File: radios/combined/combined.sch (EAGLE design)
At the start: 20 parts

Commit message: redesigned radios breakout
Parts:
- removed C1: 10uF, SparkFun-Capacitors:CAP_POL1206
- removed CONNECT, MODE: (no value), adafruit:LEDCHIPLED_0603
- removed DFU: (no value), wirepad:SMD2
- removed JP2: M11LONGPADS, SparkFun-Connectors:M11LONGPADS
- removed R1, R3: 1k, SparkFun-Resistors:RESISTOR0603
- added JP1: M11PTH, SparkFun-Connectors:M11PTH
- CLOCK, DATA, VCC: value (none) -> PAD; device wirepad:SMD2 -> ITP_Lab:PAD
- U$3: value 3.3V-REG-LARGE -> REGULATOR3.3V-UA78M33CDCYR; device ITP_Lab:3.3V-REG-LARGE -> ITP_Lab:REGULATOR3.3V-UA78M33CDCYR
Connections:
- removed net N$10: MODE.A, R3.1
- removed net N$13: DFU.P, U$4.P0.07
- removed net N$7: R1.2, U$4.P0.19
- removed net N$8: R3.2, U$4.P0.18
- removed net N$9: CONNECT.A, R1.1
- net BT-CTS: now also JP1.5; no longer JP2.10
- net BT-RTS: now also JP1.3; no longer JP2.8
- net BT-RX: now also JP1.6; no longer JP2.11
- net BT-TX: now also JP1.4; no longer JP2.9
- net GND: now also JP1.1; no longer C1.-, CONNECT.C, JP2.1, MODE.C
- net MISO: now also JP1.8; no longer JP2.4
- net MOSI: now also JP1.9; no longer JP2.5
- net N$11: now also CLOCK.P$1; no longer CLOCK.P
- net N$12: now also DATA.P$1; no longer DATA.P
- net RF-REQ: now also JP1.11; no longer JP2.7
- net RF-SS: now also JP1.10; no longer JP2.6
- net SCK: now also JP1.7; no longer JP2.3
- net VCC: now also VCC.P$1; no longer C1.+, VCC.P
- net VIN: now also JP1.2; no longer JP2.2

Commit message: about to cut board
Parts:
- removed JP1: M11PTH, SparkFun-Connectors:M11PTH
- added U$5: HEADER-11, ITP_Lab:HEADER-11
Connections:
- net BT-CTS: now also U$5.P$5; no longer JP1.5
- net BT-RTS: now also U$5.P$3; no longer JP1.3
- net BT-RX: now also U$5.P$6; no longer JP1.6
- net BT-TX: now also U$5.P$4; no longer JP1.4
- net GND: now also U$5.P$1; no longer JP1.1
- net MISO: now also U$5.P$8; no longer JP1.8
- net MOSI: now also U$5.P$9; no longer JP1.9
- net RF-REQ: now also U$5.P$11; no longer JP1.11
- net RF-SS: now also U$5.P$10; no longer JP1.10
- net SCK: now also U$5.P$7; no longer JP1.7
- net VIN: now also U$5.P$2; no longer JP1.2
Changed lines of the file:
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@@
 <part name="CLOCK" library="ITP_Lab" deviceset="PAD" device=""/>
 <part name="VCC" library="ITP_Lab" deviceset="PAD" device=""/>
-<part name="JP1" library="SparkFun-Connectors" deviceset="M11" device="PTH"/>
+<part name="U$5" library="ITP_Lab" deviceset="HEADER-11" device=""/>
 </parts>
 <sheets>
@@
 <instance part="CLOCK" gate="G$1" x="254" y="152.4"/>
 <instance part="VCC" gate="G$1" x="83.82" y="218.44" rot="R90"/>
-<instance part="JP1" gate="G$1" x="121.92" y="142.24" rot="R180"/>
+<instance part="U$5" gate="G$1" x="127" y="142.24"/>
 </instances>
 <busses>
@@
 </segment>
 <segment>
-<wire x1="111.76" y1="154.94" x2="86.36" y2="154.94" width="0.1524" layer="91"/>
+<wire x1="121.92" y1="154.94" x2="86.36" y2="154.94" width="0.1524" layer="91"/>
 <label x="93.98" y="154.94" size="1.778" layer="95" rot="R180"/>
-<pinref part="JP1" gate="G$1" pin="1"/>
+<pinref part="U$5" gate="G$1" pin="P$1"/>
 </segment>
 <segment>
@@
 <net name="VIN" class="0">
 <segment>
-<wire x1="111.76" y1="152.4" x2="86.36" y2="152.4" width="0.1524" layer="91"/>
+<wire x1="121.92" y1="152.4" x2="86.36" y2="152.4" width="0.1524" layer="91"/>
 <label x="93.98" y="152.4" size="1.778" layer="95" rot="R180"/>
-<pinref part="JP1" gate="G$1" pin="2"/>
+<pinref part="U$5" gate="G$1" pin="P$2"/>
 </segment>
 <segment>
@@
 </segment>
 <segment>
-<wire x1="111.76" y1="144.78" x2="86.36" y2="144.78" width="0.1524" layer="91"/>
+<wire x1="121.92" y1="144.78" x2="86.36" y2="144.78" width="0.1524" layer="91"/>
 <label x="93.98" y="144.78" size="1.778" layer="95" rot="R180"/>
-<pinref part="JP1" gate="G$1" pin="5"/>
+<pinref part="U$5" gate="G$1" pin="P$5"/>
 </segment>
 </net>
@@
 </segment>
 <segment>
-<wire x1="111.76" y1="147.32" x2="86.36" y2="147.32" width="0.1524" layer="91"/>
+<wire x1="121.92" y1="147.32" x2="86.36" y2="147.32" width="0.1524" layer="91"/>
 <label x="93.98" y="147.32" size="1.778" layer="95" rot="R180"/>
-<pinref part="JP1" gate="G$1" pin="4"/>
+<pinref part="U$5" gate="G$1" pin="P$4"/>
 </segment>
 </net>
@@
 </segment>
 <segment>
-<wire x1="111.76" y1="142.24" x2="86.36" y2="142.24" width="0.1524" layer="91"/>
+<wire x1="121.92" y1="142.24" x2="86.36" y2="142.24" width="0.1524" layer="91"/>
 <label x="93.98" y="142.24" size="1.778" layer="95" rot="R180"/>
-<pinref part="JP1" gate="G$1" pin="6"/>
+<pinref part="U$5" gate="G$1" pin="P$6"/>
 </segment>
 </net>
@@
 </segment>
 <segment>
-<wire x1="111.76" y1="149.86" x2="86.36" y2="149.86" width="0.1524" layer="91"/>
+<wire x1="121.92" y1="149.86" x2="86.36" y2="149.86" width="0.1524" layer="91"/>
 <label x="93.98" y="149.86" size="1.778" layer="95" rot="R180"/>
-<pinref part="JP1" gate="G$1" pin="3"/>
+<pinref part="U$5" gate="G$1" pin="P$3"/>
 </segment>
 </net>
@@
 </segment>
 <segment>
-<wire x1="111.76" y1="129.54" x2="86.36" y2="129.54" width="0.1524" layer="91"/>
+<wire x1="121.92" y1="129.54" x2="86.36" y2="129.54" width="0.1524" layer="91"/>
 <label x="93.98" y="129.54" size="1.778" layer="95" rot="R180"/>
-<pinref part="JP1" gate="G$1" pin="11"/>
+<pinref part="U$5" gate="G$1" pin="P$11"/>
 </segment>
 </net>
@@
 </segment>
 <segment>
-<wire x1="111.76" y1="132.08" x2="86.36" y2="132.08" width="0.1524" layer="91"/>
+<wire x1="121.92" y1="132.08" x2="86.36" y2="132.08" width="0.1524" layer="91"/>
 <label x="93.98" y="132.08" size="1.778" layer="95" rot="R180"/>
-<pinref part="JP1" gate="G$1" pin="10"/>
+<pinref part="U$5" gate="G$1" pin="P$10"/>
 </segment>
 </net>
@@
 </segment>
 <segment>
-<wire x1="111.76" y1="134.62" x2="86.36" y2="134.62" width="0.1524" layer="91"/>
+<wire x1="121.92" y1="134.62" x2="86.36" y2="134.62" width="0.1524" layer="91"/>
 <label x="93.98" y="134.62" size="1.778" layer="95" rot="R180"/>
-<pinref part="JP1" gate="G$1" pin="9"/>
+<pinref part="U$5" gate="G$1" pin="P$9"/>
 </segment>
 </net>
@@
 </segment>
 <segment>
-<wire x1="111.76" y1="137.16" x2="86.36" y2="137.16" width="0.1524" layer="91"/>
+<wire x1="121.92" y1="137.16" x2="86.36" y2="137.16" width="0.1524" layer="91"/>
 <label x="93.98" y="137.16" size="1.778" layer="95" rot="R180"/>
-<pinref part="JP1" gate="G$1" pin="8"/>
+<pinref part="U$5" gate="G$1" pin="P$8"/>
 </segment>
 </net>
@@
 </segment>
 <segment>
-<wire x1="111.76" y1="139.7" x2="86.36" y2="139.7" width="0.1524" layer="91"/>
+<wire x1="121.92" y1="139.7" x2="86.36" y2="139.7" width="0.1524" layer="91"/>
 <label x="93.98" y="139.7" size="1.778" layer="95" rot="R180"/>
-<pinref part="JP1" gate="G$1" pin="7"/>
-</segment>
-</net>
+<pinref part="U$5" gate="G$1" pin="P$7"/>
+</segment>
+</net>

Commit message: updated so nrf51 uses SPI instead of UART
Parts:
- removed DATA: PAD, ITP_Lab:PAD
- removed R5: 100k, SparkFun-Resistors:RESISTOR0603
- removed U$4: MDBT40, ITP_Lab:MDBT40
- added C1: 10uF, SparkFun-Capacitors:CAP_POL1206
- added CONNECTED: (no value), adafruit:LEDCHIP-LED0603
- added JP1: M02PTH, SparkFun-Connectors:M02PTH
- added JP3: (no value), SparkFun-Connectors:M08NO_SILK
- added R1, R3: 10k, SparkFun-Resistors:RESISTOR0603
- C10: value 0.1uF -> 1uF
- R2: value (none) -> 10k
- R4: value 100k -> 10k; device SparkFun-Resistors:RESISTOR0603 -> adafruit:R-US_R0603
- U$5: value HEADER-11 -> NRF51-MDBT40-SPI; device ITP_Lab:HEADER-11 -> ITP_Lab:NRF51-MDBT40-SPI
- renumbered LED1 to POWER
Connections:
- removed net BT-CTS: R5.2, U$4.P0.10, U$5.P$5
- removed net BT-RTS: U$4.P0.08, U$5.P$3
- removed net BT-RX: R4.2, U$4.P0.11, U$5.P$6
- removed net BT-TX: U$4.P0.09, U$5.P$4
- removed net N$12: DATA.P$1, U$4.SWDIO
- new net BT-REQ: JP3.2, U$5.P0.25
- new net BT-SS: JP3.5, R3.2, U$5.P0.24
- new net N$2: R4.1, U$5.P0.19
- new net N$4: CONNECTED.A, R4.2
- new net SWDIO/RST: JP3.3, R1.2, U$5.SWDIO
- net GND: now also C1.-, CONNECTED.C, JP1.1, U$5.GND1, U$5.GND2, U$5.GND3, U$5.GND4, U$5.GND5, U$5.P0.30; no longer U$4.GND1, U$4.GND2, U$4.GND3, U$4.GND4, U$4.GND5, U$4.P0.30, U$5.P$1
- net MISO: now also JP3.7, U$5.P0.22; no longer U$5.P$8
- net MOSI: now also JP3.6, U$5.P0.23; no longer U$5.P$9
- net N$11: now also U$5.SWCLK; no longer U$4.SWCLK
- net RF-REQ: now also JP3.1; no longer U$5.P$11
- net RF-SS: now also JP3.4; no longer U$5.P$10
- net SCK: now also JP3.8, U$5.P0.21; no longer U$5.P$7
- net VCC: now also R1.1, R3.1, U$5.AVDD, U$5.VDD; no longer R4.1, R5.1, U$4.AVDD, U$4.P0.01, U$4.VDD
- net VIN: now also C1.+, JP1.2; no longer U$5.P$2
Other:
- moved on the sheet: R4

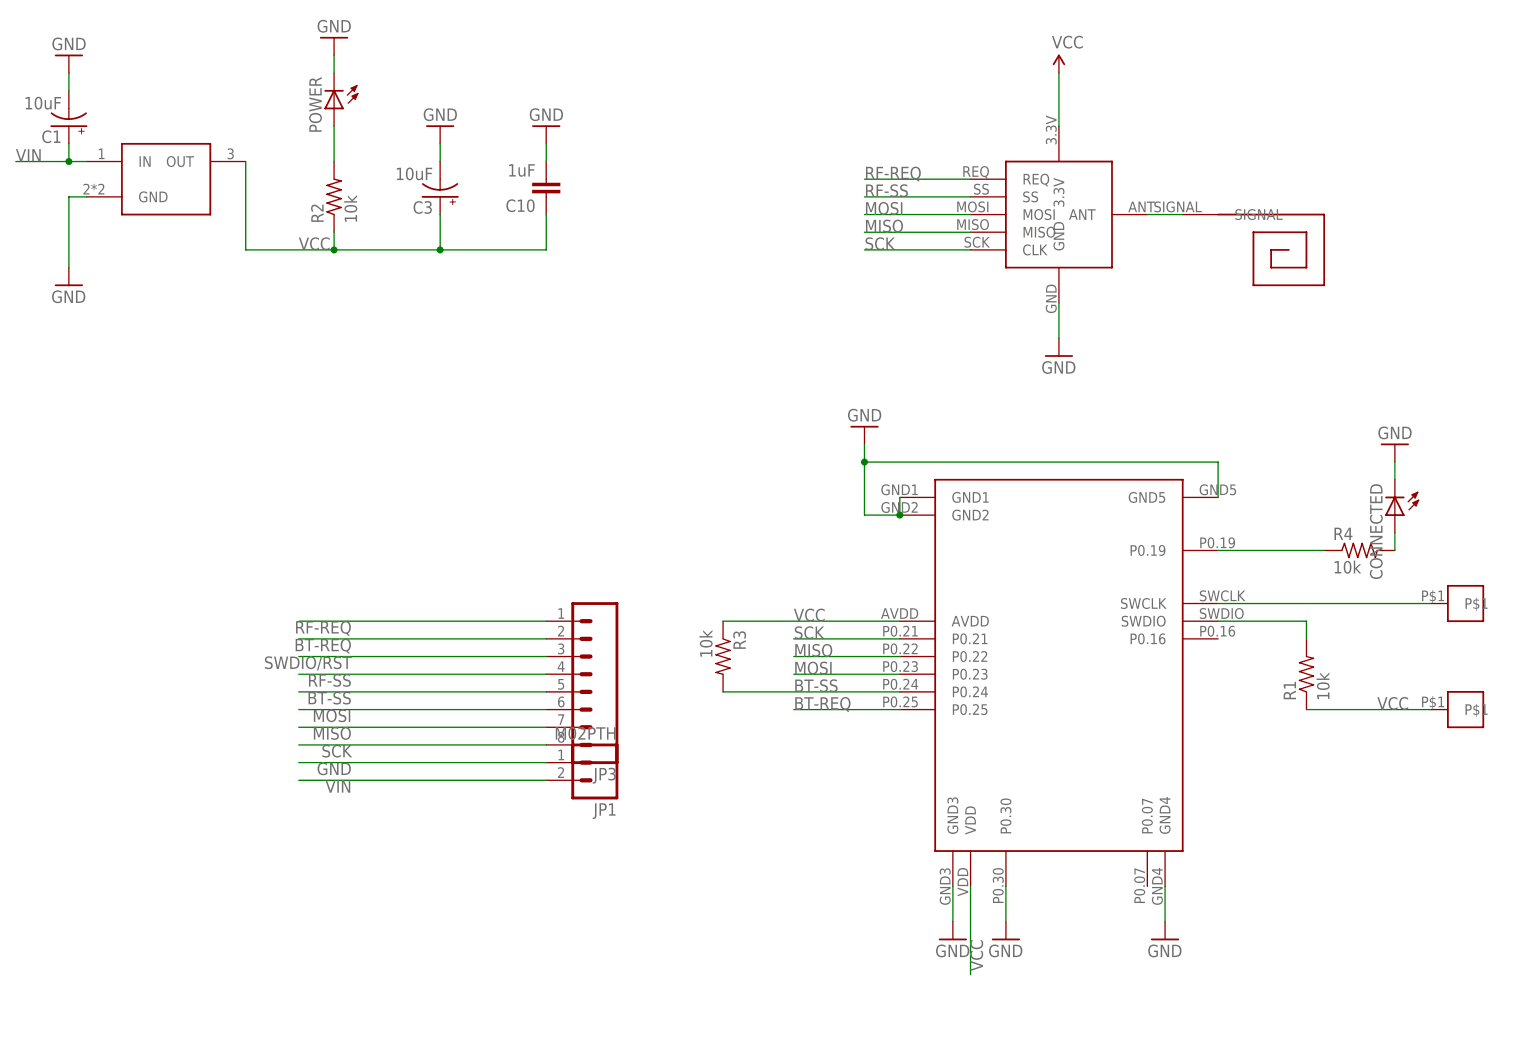
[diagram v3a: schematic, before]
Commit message: SPI combined board ready to print
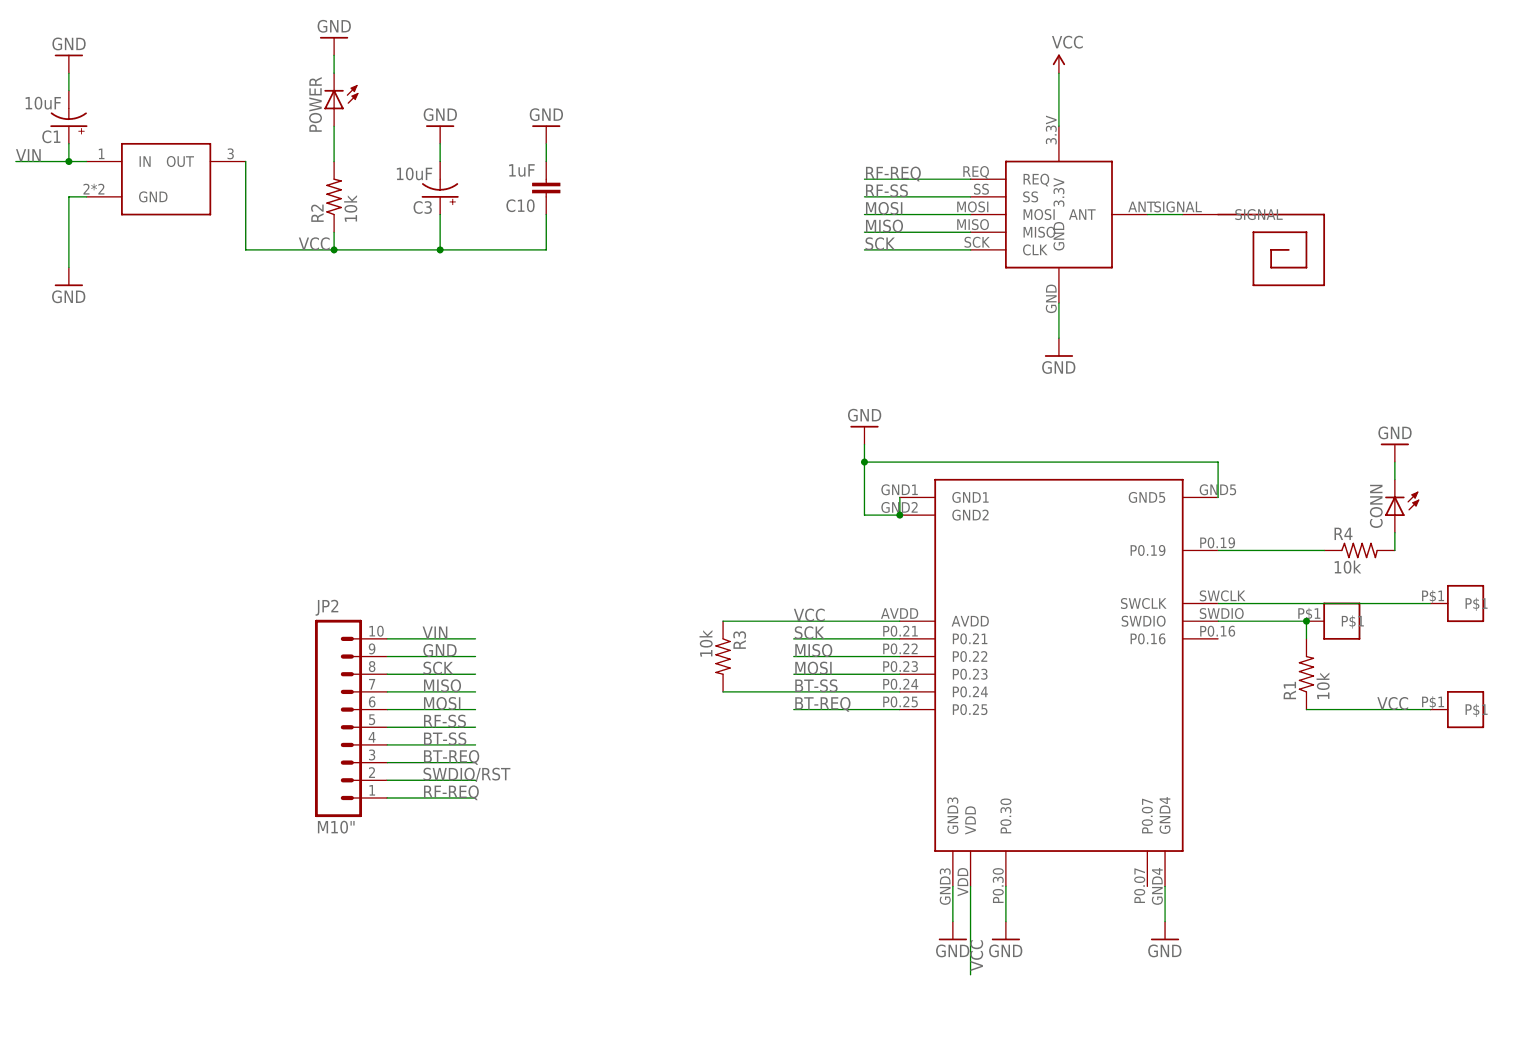
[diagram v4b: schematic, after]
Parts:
- removed JP1: M02PTH, SparkFun-Connectors:M02PTH
- removed JP3: (no value), SparkFun-Connectors:M08NO_SILK
- added CLOCK1: PAD, ITP_Lab:PAD
- added JP2: M10", SparkFun-Connectors:M10"
- renumbered CONNECTED to CONN
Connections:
- net BT-REQ: now also JP2.3; no longer JP3.2
- net BT-SS: now also JP2.4; no longer JP3.5
- net GND: now also JP2.9; no longer JP1.1
- net MISO: now also JP2.7; no longer JP3.7
- net MOSI: now also JP2.6; no longer JP3.6
- net RF-REQ: now also JP2.1; no longer JP3.1
- net RF-SS: now also JP2.5; no longer JP3.4
- net SCK: now also JP2.8; no longer JP3.8
- net SWDIO/RST: now also CLOCK1.P$1, JP2.2; no longer JP3.3
- net VIN: now also JP2.10; no longer JP1.2
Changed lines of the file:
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@@
 <part name="R3" library="SparkFun-Resistors" deviceset="RESISTOR" device="0603" value="10k"/>
 <part name="R4" library="adafruit" deviceset="R-US_" device="R0603" value="10k"/>
-<part name="CONNECTED" library="adafruit" deviceset="LED" device="CHIP-LED0603"/>
+<part name="CONN" library="adafruit" deviceset="LED" device="CHIP-LED0603"/>
 <part name="GND4" library="SparkFun" deviceset="GND" device=""/>
 <part name="U$5" library="ITP_Lab" deviceset="NRF51-MDBT40-SPI" device=""/>
-<part name="JP1" library="SparkFun-Connectors" deviceset="M02" device="PTH"/>
-<part name="JP3" library="SparkFun-Connectors" deviceset="M08" device="NO_SILK"/>
+<part name="JP2" library="SparkFun-Connectors" deviceset="M10" device="&quot;"/>
+<part name="CLOCK1" library="ITP_Lab" deviceset="PAD" device=""/>
 </parts>
 <sheets>
@@
 <instance part="R3" gate="G$1" x="147.32" y="144.78" rot="R270"/>
 <instance part="R4" gate="G$1" x="238.76" y="160.02"/>
-<instance part="CONNECTED" gate="G$1" x="243.84" y="165.1" rot="R180"/>
+<instance part="CONN" gate="G$1" x="243.84" y="165.1" rot="R180"/>
 <instance part="GND4" gate="1" x="243.84" y="175.26" rot="R180"/>
 <instance part="U$5" gate="G$1" x="195.58" y="142.24"/>
-<instance part="JP1" gate="G$1" x="129.54" y="129.54" rot="R180"/>
-<instance part="JP3" gate="G$1" x="127" y="142.24" rot="R180"/>
+<instance part="JP2" gate="G$1" x="88.9" y="142.24"/>
+<instance part="CLOCK1" gate="G$1" x="236.22" y="149.86"/>
 </instances>
 <busses>
@@
 </segment>
 <segment>
-<wire x1="121.92" y1="129.54" x2="86.36" y2="129.54" width="0.1524" layer="91"/>
-<label x="93.98" y="129.54" size="1.778" layer="95" rot="R180"/>
-<pinref part="JP1" gate="G$1" pin="1"/>
+<wire x1="99.06" y1="144.78" x2="111.76" y2="144.78" width="0.1524" layer="91"/>
+<label x="104.14" y="144.78" size="1.778" layer="95"/>
+<pinref part="JP2" gate="G$1" pin="9"/>
 </segment>
 <segment>
@@
 <segment>
 <pinref part="GND4" gate="1" pin="GND"/>
-<pinref part="CONNECTED" gate="G$1" pin="C"/>
+<pinref part="CONN" gate="G$1" pin="C"/>
 <wire x1="243.84" y1="172.72" x2="243.84" y2="170.18" width="0.1524" layer="91"/>
 </segment>
@@
 </segment>
 <segment>
-<wire x1="121.92" y1="127" x2="86.36" y2="127" width="0.1524" layer="91"/>
-<label x="93.98" y="127" size="1.778" layer="95" rot="R180"/>
-<pinref part="JP1" gate="G$1" pin="2"/>
+<wire x1="99.06" y1="147.32" x2="111.76" y2="147.32" width="0.1524" layer="91"/>
+<label x="104.14" y="147.32" size="1.778" layer="95"/>
+<pinref part="JP2" gate="G$1" pin="10"/>
 </segment>
 </net>
@@
 </segment>
 <segment>
-<wire x1="121.92" y1="149.86" x2="86.36" y2="149.86" width="0.1524" layer="91"/>
-<label x="93.98" y="149.86" size="1.778" layer="95" rot="R180"/>
-<pinref part="JP3" gate="G$1" pin="1"/>
+<wire x1="99.06" y1="124.46" x2="111.76" y2="124.46" width="0.1524" layer="91"/>
+<label x="104.14" y="124.46" size="1.778" layer="95"/>
+<pinref part="JP2" gate="G$1" pin="1"/>
 </segment>
 </net>
@@
 </segment>
 <segment>
-<wire x1="121.92" y1="142.24" x2="86.36" y2="142.24" width="0.1524" layer="91"/>
-<label x="93.98" y="142.24" size="1.778" layer="95" rot="R180"/>
-<pinref part="JP3" gate="G$1" pin="4"/>
+<wire x1="99.06" y1="134.62" x2="111.76" y2="134.62" width="0.1524" layer="91"/>
+<label x="104.14" y="134.62" size="1.778" layer="95"/>
+<pinref part="JP2" gate="G$1" pin="5"/>
 </segment>
 </net>
@@
 <wire x1="231.14" y1="149.86" x2="231.14" y2="147.32" width="0.1524" layer="91"/>
 <pinref part="U$5" gate="G$1" pin="SWDIO"/>
-</segment>
-<segment>
-<wire x1="121.92" y1="144.78" x2="86.36" y2="144.78" width="0.1524" layer="91"/>
-<label x="93.98" y="144.78" size="1.778" layer="95" rot="R180"/>
-<pinref part="JP3" gate="G$1" pin="3"/>
+<pinref part="CLOCK1" gate="G$1" pin="P$1"/>
+<junction x="231.14" y="149.86"/>
+</segment>
+<segment>
+<wire x1="99.06" y1="127" x2="111.76" y2="127" width="0.1524" layer="91"/>
+<label x="104.14" y="127" size="1.778" layer="95"/>
+<pinref part="JP2" gate="G$1" pin="2"/>
 </segment>
 </net>
@@
 </segment>
 <segment>
-<wire x1="121.92" y1="137.16" x2="86.36" y2="137.16" width="0.1524" layer="91"/>
-<label x="93.98" y="137.16" size="1.778" layer="95" rot="R180"/>
-<pinref part="JP3" gate="G$1" pin="6"/>
+<wire x1="99.06" y1="137.16" x2="111.76" y2="137.16" width="0.1524" layer="91"/>
+<label x="104.14" y="137.16" size="1.778" layer="95"/>
+<pinref part="JP2" gate="G$1" pin="6"/>
 </segment>
 <segment>
@@
 </segment>
 <segment>
-<wire x1="121.92" y1="134.62" x2="86.36" y2="134.62" width="0.1524" layer="91"/>
-<label x="93.98" y="134.62" size="1.778" layer="95" rot="R180"/>
-<pinref part="JP3" gate="G$1" pin="7"/>
+<wire x1="99.06" y1="139.7" x2="111.76" y2="139.7" width="0.1524" layer="91"/>
+<label x="104.14" y="139.7" size="1.778" layer="95"/>
+<pinref part="JP2" gate="G$1" pin="7"/>
 </segment>
 <segment>
@@
 </segment>
 <segment>
-<wire x1="121.92" y1="132.08" x2="86.36" y2="132.08" width="0.1524" layer="91"/>
-<label x="93.98" y="132.08" size="1.778" layer="95" rot="R180"/>
-<pinref part="JP3" gate="G$1" pin="8"/>
+<wire x1="99.06" y1="142.24" x2="111.76" y2="142.24" width="0.1524" layer="91"/>
+<label x="104.14" y="142.24" size="1.778" layer="95"/>
+<pinref part="JP2" gate="G$1" pin="8"/>
 </segment>
 <segment>
@@
 <net name="BT-REQ" class="0">
 <segment>
-<wire x1="121.92" y1="147.32" x2="86.36" y2="147.32" width="0.1524" layer="91"/>
-<label x="93.98" y="147.32" size="1.778" layer="95" rot="R180"/>
-<pinref part="JP3" gate="G$1" pin="2"/>
-</segment>
-<segment>
 <wire x1="172.72" y1="137.16" x2="157.48" y2="137.16" width="0.1524" layer="91"/>
 <label x="157.48" y="137.16" size="1.778" layer="95"/>
 <pinref part="U$5" gate="G$1" pin="P0.25"/>
 </segment>
+<segment>
+<wire x1="99.06" y1="129.54" x2="111.76" y2="129.54" width="0.1524" layer="91"/>
+<label x="104.14" y="129.54" size="1.778" layer="95"/>
+<pinref part="JP2" gate="G$1" pin="3"/>
+</segment>
 </net>
 <net name="BT-SS" class="0">
-<segment>
-<wire x1="121.92" y1="139.7" x2="86.36" y2="139.7" width="0.1524" layer="91"/>
-<label x="93.98" y="139.7" size="1.778" layer="95" rot="R180"/>
-<pinref part="JP3" gate="G$1" pin="5"/>
-</segment>
 <segment>
 <pinref part="R3" gate="G$1" pin="2"/>
@@
 <label x="157.48" y="139.7" size="1.778" layer="95"/>
 </segment>
+<segment>
+<wire x1="99.06" y1="132.08" x2="111.76" y2="132.08" width="0.1524" layer="91"/>
+<label x="104.14" y="132.08" size="1.778" layer="95"/>
+<pinref part="JP2" gate="G$1" pin="4"/>
+</segment>
 </net>
 <net name="N$2" class="0">
@@
 <net name="N$4" class="0">
 <segment>
-<pinref part="CONNECTED" gate="G$1" pin="A"/>
+<pinref part="CONN" gate="G$1" pin="A"/>
 <pinref part="R4" gate="G$1" pin="2"/>
 <wire x1="243.84" y1="162.56" x2="243.84" y2="160.02" width="0.1524" layer="91"/>
